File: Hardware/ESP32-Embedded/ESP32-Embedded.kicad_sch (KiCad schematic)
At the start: 27 parts, among them J1 Micro USB, Q1 S8050, Q2 S8050, SW1 SW_Push, SW2 SW_Push, U1 ESP32-WROOM-32E, U2 AMS1117-3.3, U3 CH340G, Y1 12Mhz

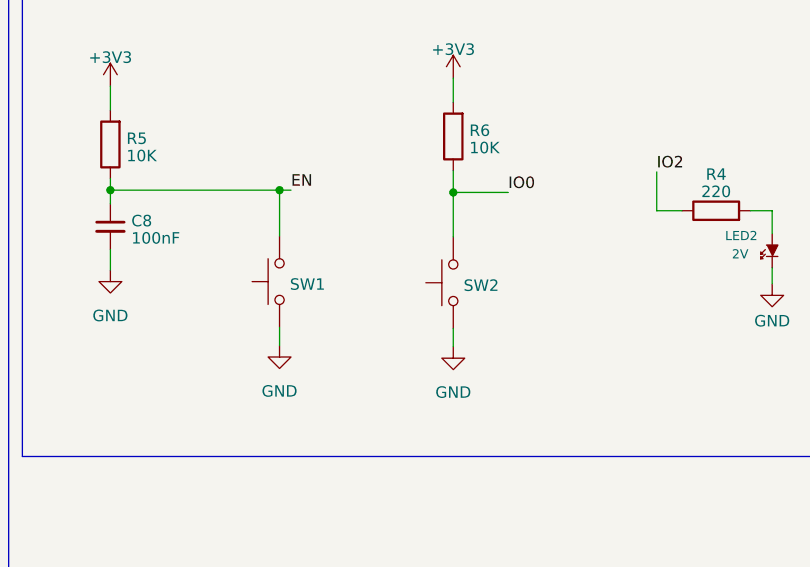
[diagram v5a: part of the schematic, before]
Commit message: Hice cambios de tamaño de pistas y margen de gnd añadi 3d a componentes y agregue imagenes de los 3D
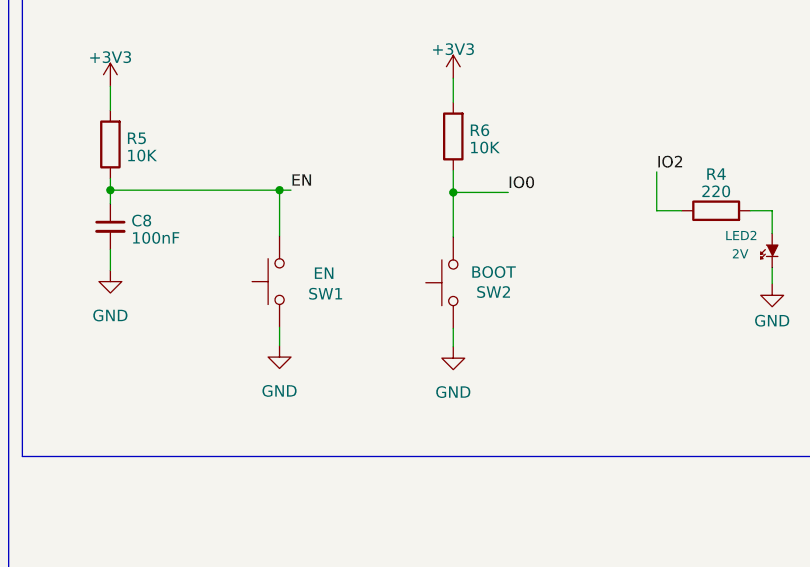
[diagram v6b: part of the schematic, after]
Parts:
- SW1: value SW_Push -> EN
- SW2: value SW_Push -> BOOT
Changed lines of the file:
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@@
   )
   (symbol (lib_id "EESTN5:SW_Push") (at 240.665 54.737 90) (unit 1)
-    (in_bom yes) (on_board yes) (dnp no) (fields_autoplaced)
-    (property "Reference" "SW2" (at 241.808 55.0538 90)
+    (in_bom yes) (on_board yes) (dnp no)
+    (property "Reference" "SW2" (at 243.205 55.8158 90)
       (effects (font (size 1.27 1.27)) (justify right))
     )
-    (property "Value" "SW_Push" (at 242.189 54.737 0)
-      (effects (font (size 1.27 1.27)) hide)
+    (property "Value" "BOOT" (at 245.11 53.594 90)
+      (effects (font (size 1.27 1.27)))
     )
     (property "Footprint" "Button_Switch_SMD:SW_SPST_B3U-1000P-B" (at 235.585 54.737 0)
@@
   )
   (symbol (lib_id "EESTN5:SW_Push") (at 221.361 54.61 90) (unit 1)
-    (in_bom yes) (on_board yes) (dnp no) (fields_autoplaced)
-    (property "Reference" "SW1" (at 222.504 54.9268 90)
+    (in_bom yes) (on_board yes) (dnp no)
+    (property "Reference" "SW1" (at 224.536 56.007 90)
       (effects (font (size 1.27 1.27)) (justify right))
     )
-    (property "Value" "SW_Push" (at 222.885 54.61 0)
-      (effects (font (size 1.27 1.27)) hide)
+    (property "Value" "EN" (at 226.314 53.721 90)
+      (effects (font (size 1.27 1.27)))
     )
     (property "Footprint" "Button_Switch_SMD:SW_SPST_B3U-1000P-B" (at 216.281 54.61 0)

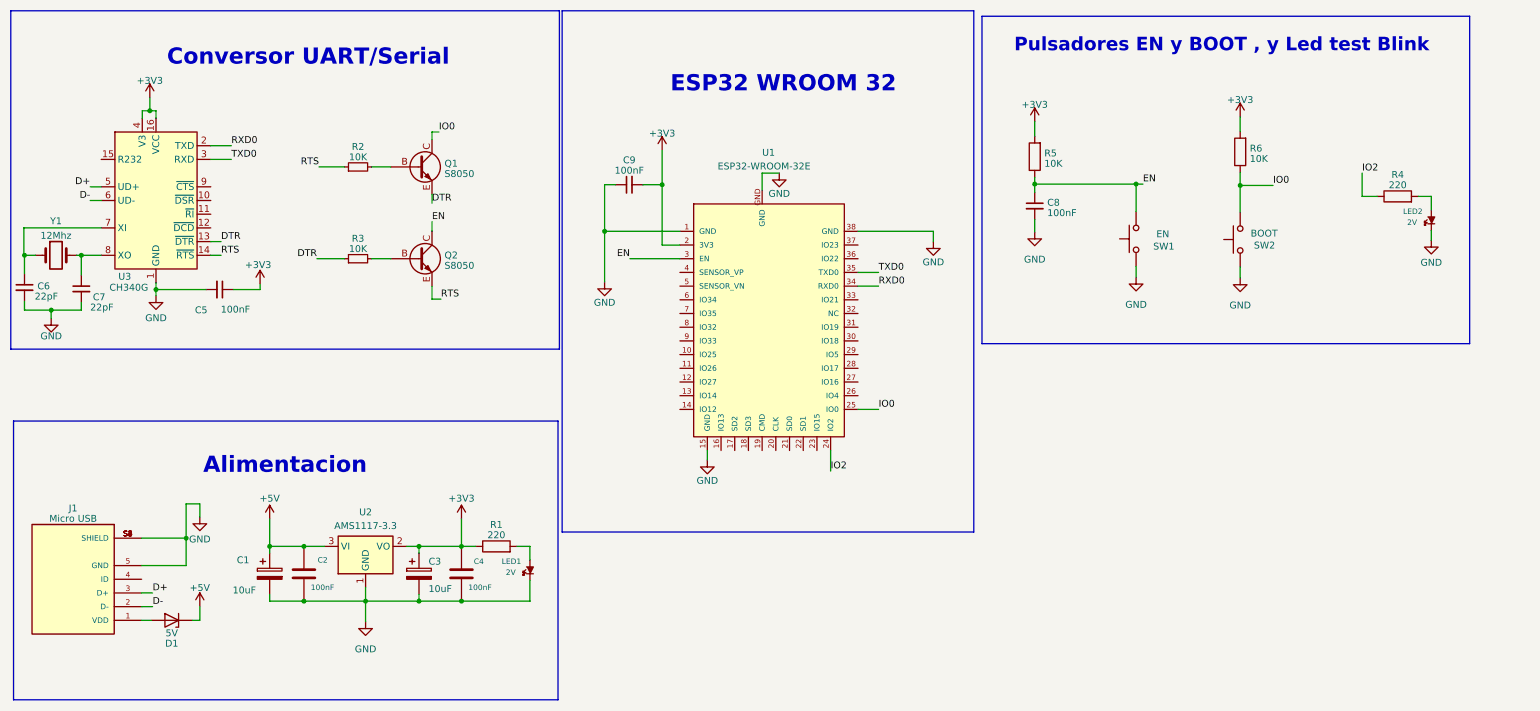
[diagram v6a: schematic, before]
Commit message: Cambios importantes correcciones con Bustos placa lista
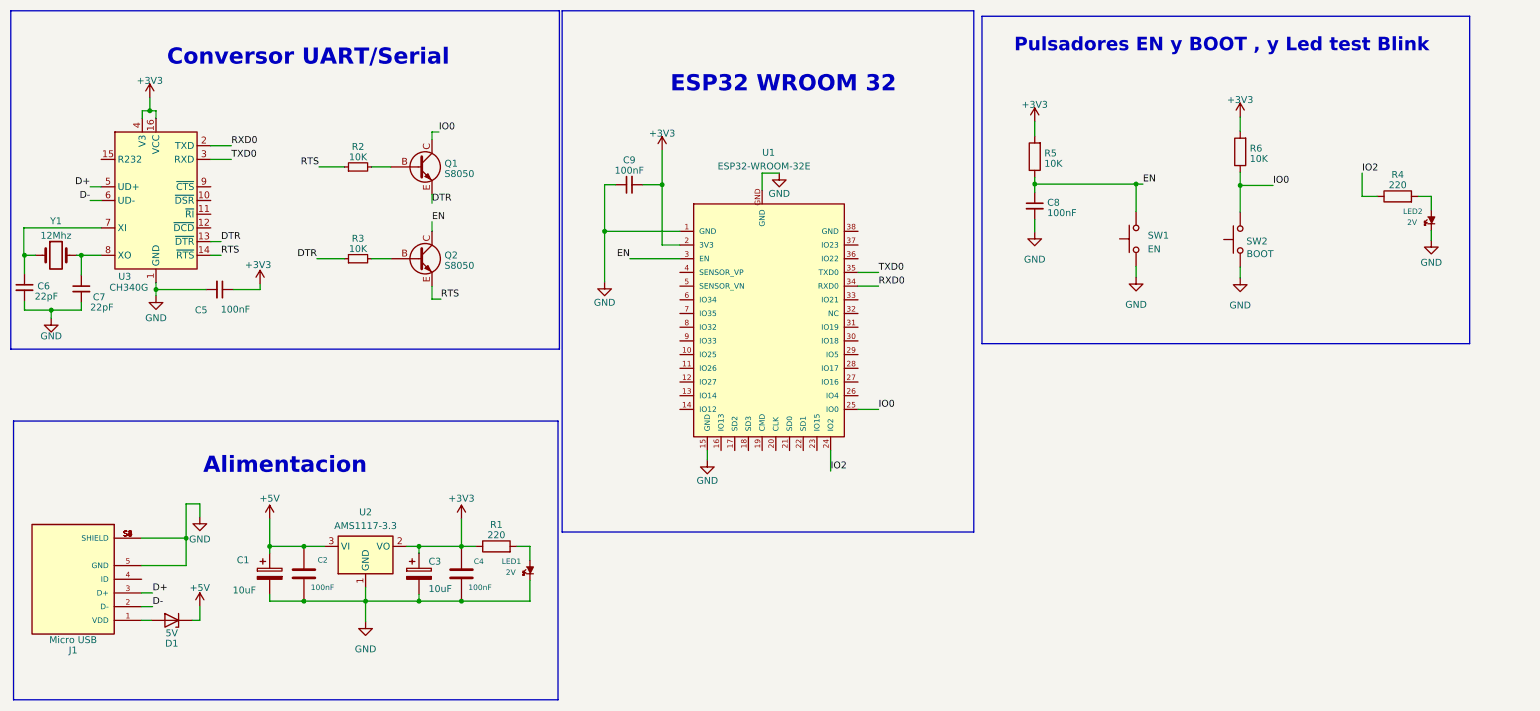
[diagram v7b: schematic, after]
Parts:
- C1, C3: footprint Capacitor_THT:CP_Radial_D4.0mm_P1.50mm -> EESTN5:CAP_ELEC_SMD_4X5.5
- R2, R3: footprint EESTN5:RES0.2 -> EESTN5:R_1206
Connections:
- net GND: no longer U1.38 (GND)
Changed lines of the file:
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@@
     (stroke (width 0) (type default))
   )
-  (wire (pts (xy 169.799 53.213) (xy 183.769 53.213))
-    (stroke (width 0) (type default))
-  )
   (wire (pts (xy 96.266 111.633) (xy 98.933 111.633))
     (stroke (width 0) (type default))
@@
     (stroke (width 0) (type default))
   )
-  (wire (pts (xy 183.769 53.213) (xy 183.769 55.118))
-    (stroke (width 0) (type default))
-  )
   (wire (pts (xy 37.084 30.861) (xy 37.084 32.258))
     (stroke (width 0) (type default))
@@
       (effects (font (size 1.27 1.27)) (justify left))
     )
-    (property "Footprint" "Capacitor_THT:CP_Radial_D4.0mm_P1.50mm" (at 61.6712 120.523 0)
+    (property "Footprint" "EESTN5:CAP_ELEC_SMD_4X5.5" (at 61.6712 120.523 0)
       (effects (font (size 1.27 1.27)) hide)
     )
@@
   (symbol (lib_id "MICROUSB:10103592-0001LF") (at 24.257 117.729 180) (unit 1)
     (in_bom yes) (on_board yes) (dnp no) (fields_autoplaced)
-    (property "Reference" "J1" (at 24.257 104.5591 0)
+    (property "Reference" "J1" (at 24.257 130.8989 0)
       (effects (font (size 1.27 1.27)))
     )
-    (property "Value" "Micro USB" (at 24.257 106.4801 0)
+    (property "Value" "Micro USB" (at 24.257 128.9779 0)
       (effects (font (size 1.27 1.27)))
     )
@@
     (pin "4")
     (pin "5")
-    (pin "S1")
     (pin "S2")
     (pin "S3")
@@
     (pin "S5")
     (pin "S6")
+    (pin "S1")
     (instances
       (project "ESP32-Embedded"
@@
       (effects (font (size 1.27 1.27)))
     )
-    (property "Footprint" "EESTN5:RES0.2" (at 77.089 41.275 0)
+    (property "Footprint" "EESTN5:R_1206" (at 77.089 41.275 0)
       (effects (font (size 1.27 1.27)) hide)
     )
@@
       (effects (font (size 1.27 1.27)))
     )
-    (property "Footprint" "EESTN5:RES0.2" (at 77.089 58.293 0)
+    (property "Footprint" "EESTN5:R_1206" (at 77.089 58.293 0)
       (effects (font (size 1.27 1.27)) hide)
     )
@@
   (symbol (lib_id "EESTN5:SW_Push") (at 240.665 54.737 90) (unit 1)
     (in_bom yes) (on_board yes) (dnp no)
-    (property "Reference" "SW2" (at 243.205 55.8158 90)
+    (property "Reference" "SW2" (at 241.808 55.0538 90)
       (effects (font (size 1.27 1.27)) (justify right))
     )
-    (property "Value" "BOOT" (at 245.11 53.594 90)
+    (property "Value" "BOOT" (at 244.348 57.404 90)
       (effects (font (size 1.27 1.27)))
     )
@@
   )
   (symbol (lib_id "EESTN5:SW_Push") (at 221.361 54.61 90) (unit 1)
-    (in_bom yes) (on_board yes) (dnp no)
-    (property "Reference" "SW1" (at 224.536 56.007 90)
+    (in_bom yes) (on_board yes) (dnp no) (fields_autoplaced)
+    (property "Reference" "SW1" (at 223.52 53.975 90)
       (effects (font (size 1.27 1.27)) (justify right))
     )
-    (property "Value" "EN" (at 226.314 53.721 90)
-      (effects (font (size 1.27 1.27)))
+    (property "Value" "EN" (at 223.52 56.515 90)
+      (effects (font (size 1.27 1.27)) (justify right))
     )
     (property "Footprint" "Button_Switch_SMD:SW_SPST_B3U-1000P-B" (at 216.281 54.61 0)
@@
     )
   )
-  (symbol (lib_id "power:GND") (at 183.769 55.118 0) (unit 1)
-    (in_bom yes) (on_board yes) (dnp no)
-    (property "Reference" "#PWR04" (at 183.769 61.468 0)
-      (effects (font (size 1.27 1.27)) hide)
-    )
-    (property "Value" "GND" (at 183.769 58.928 0)
-      (effects (font (size 1.27 1.27)))
-    )
-    (property "Footprint" "" (at 183.769 55.118 0)
-      (effects (font (size 1.27 1.27)) hide)
-    )
-    (property "Datasheet" "" (at 183.769 55.118 0)
-      (effects (font (size 1.27 1.27)) hide)
-    )
-    (pin "1")
-    (instances
-      (project "ESP32-Embedded"
-        (path "/44ee4593-0772-40e5-aa53-983b9011845a"
-          (reference "#PWR04") (unit 1)
-        )
-      )
-      (project "Esp32Modulo"
-        (path "/d8ce7d9a-219e-40d1-b957-d72bdccbdc30"
-          (reference "#PWR09") (unit 1)
-        )
-      )
-    )
-  )
   (symbol (lib_id "Device:C_Small") (at 51.435 64.008 270) (unit 1)
     (in_bom yes) (on_board yes) (dnp no)
@@
       (effects (font (size 1.27 1.27)) (justify left))
     )
-    (property "Footprint" "Capacitor_THT:CP_Radial_D4.0mm_P1.50mm" (at 89.3572 120.523 0)
+    (property "Footprint" "EESTN5:CAP_ELEC_SMD_4X5.5" (at 89.3572 120.523 0)
       (effects (font (size 1.27 1.27)) hide)
     )

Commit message: Cambios de encapsulados
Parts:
- LED1, LED2: footprint EESTN5:LED_1206 -> EESTN5:R_0805
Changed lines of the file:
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@@
       (effects (font (size 1.016 1.016)))
     )
-    (property "Footprint" "EESTN5:LED_1206" (at 276.098 50.546 0)
+    (property "Footprint" "EESTN5:R_0805" (at 276.098 50.546 0)
       (effects (font (size 1.524 1.524)) hide)
     )
@@
       (effects (font (size 1.016 1.016)))
     )
-    (property "Footprint" "EESTN5:LED_1206" (at 108.966 115.443 0)
+    (property "Footprint" "EESTN5:R_0805" (at 108.966 115.443 0)
       (effects (font (size 1.524 1.524)) hide)
     )
